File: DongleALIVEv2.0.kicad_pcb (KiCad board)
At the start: 2 copper layers, 45 x 55 mm, 76 parts, among them J1 C-OBD-II-16M, J2 Conn_01x05_Socket, J3 Conn_01x05_Socket, J4 USB_B_Micro, Q1 IRF5305S, Q2 SS8050-G, Q3 SS8050-G, SW1 SW_Push, SW2 SW_Push, SW3 SW_SPDT_321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

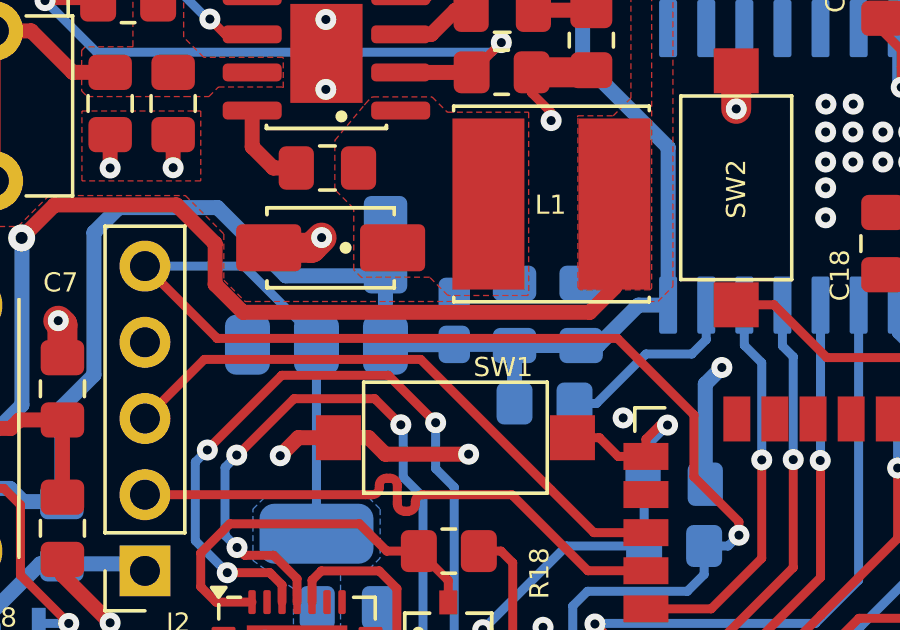
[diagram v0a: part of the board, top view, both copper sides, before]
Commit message: Fix tantalum capacitor & JLCPCB codes
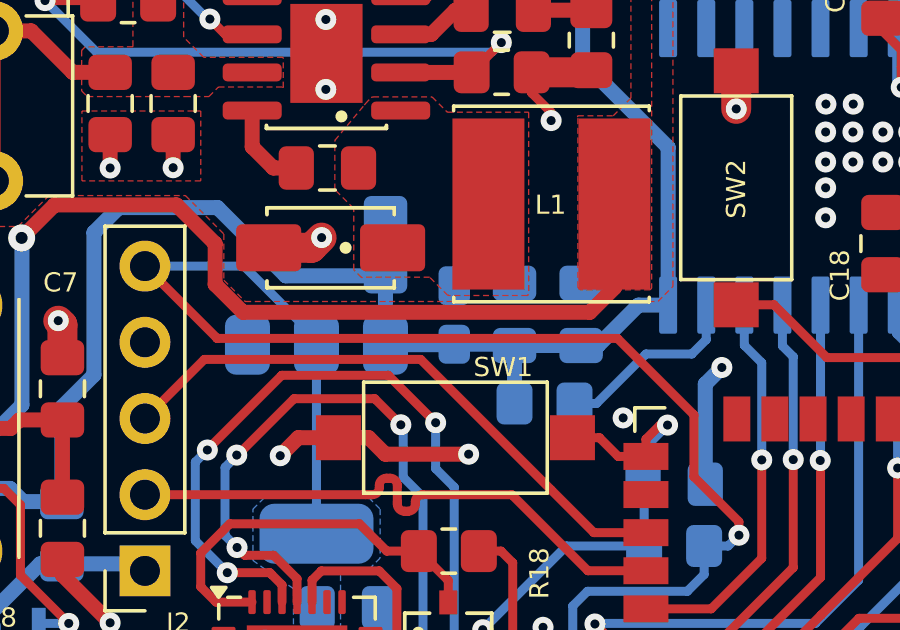
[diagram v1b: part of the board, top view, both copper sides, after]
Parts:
- C15, C17: value 0.1uF -> 100nF
- C16: footprint Capacitor_Tantalum_SMD:CP_EIA-1608-08_AVX-J_Pad1.25x1.05mm_HandSolder -> Capacitor_Tantalum_SMD:CP_EIA-2012-12_Kemet-R_Pad1.30x1.05mm_HandSolder
- moved C16 0.18 mm to (175.0, 95.8)

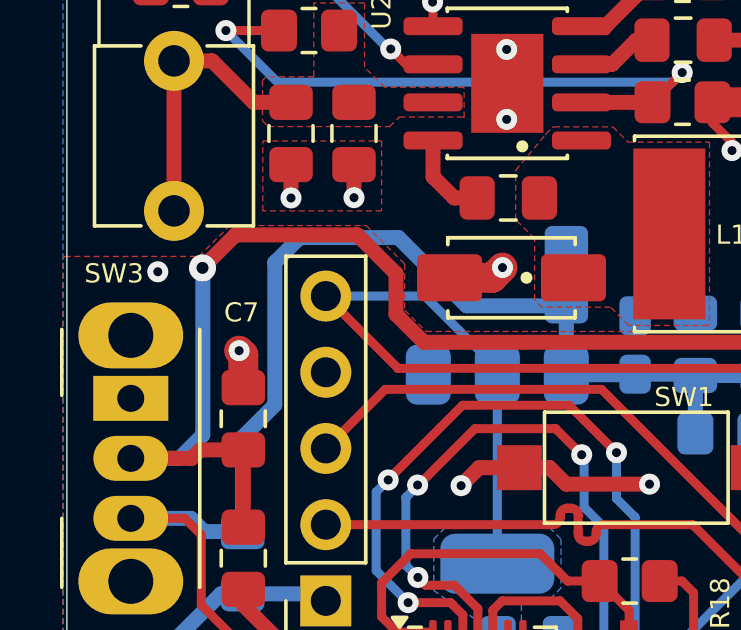
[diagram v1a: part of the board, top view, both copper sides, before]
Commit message: Testpoint to Vout
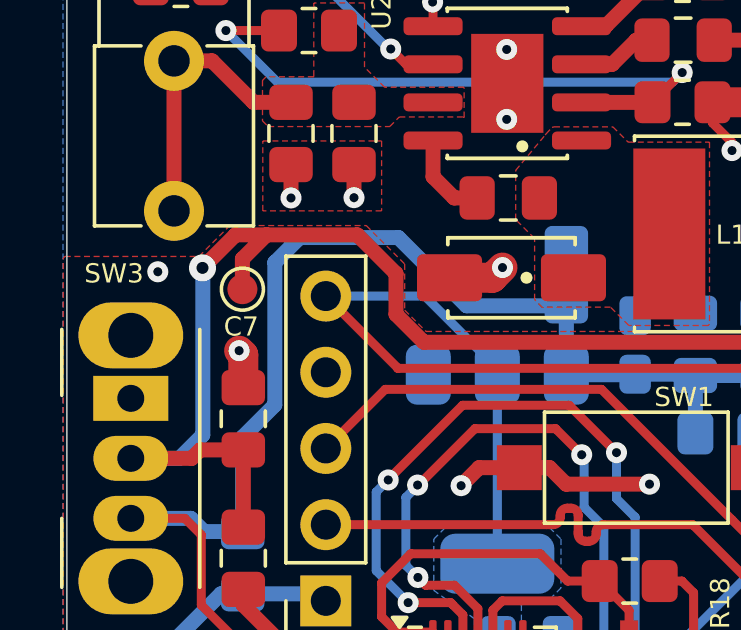
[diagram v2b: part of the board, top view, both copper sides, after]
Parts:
- added TP1: TestPoint, TestPoint:TestPoint_Pad_D1.0mm, F.Cu at (161.9, 93.9)
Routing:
- net /VoltageRegulatorESD/Vout: track 40.4 -> 42.5 mm
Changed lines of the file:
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@@
 		(allow_soldermask_bridges_in_footprints no)
 		(pcbplotparams
-			(layerselection 0x0000010_ffffffff)
+			(layerselection 0x00010fc_ffffffff)
 			(plot_on_all_layers_selection 0x0000000_00000000)
 			(disableapertmacros no)
@@
 			(sketchpadsonfab no)
 			(subtractmaskfromsilk no)
-			(outputformat 4)
+			(outputformat 1)
 			(mirror no)
-			(drillshape 2)
+			(drillshape 0)
 			(scaleselection 1)
-			(outputdirectory "01_Specs/02_LayoutPCB/")
+			(outputdirectory "02_Gerber&BOM/01_Gerber/00_Drill_Files/")
 		)
 	)
@@
 		(tags "capacitor handsolder")
 		(property "Reference" "C7"
-			(at 3.54 -0.06 180)
+			(at 3.07 -0.07 180)
 			(layer "F.SilkS")
 			(effects
@@
 			)
 		)
-		(property "LCSC" ""
+		(property "LCSC" "C157623"
 			(at 0 0 -90)
 			(unlocked yes)
@@
 		)
 	)
+	(footprint "TestPoint:TestPoint_Pad_D1.0mm"
+		(layer "F.Cu")
+		(at 161.93 93.91)
+		(descr "SMD pad as test Point, diameter 1.0mm")
+		(tags "test point SMD pad")
+		(property "Reference" "TP1"
+			(at 0 -1.448 0)
+			(layer "F.SilkS")
+			(hide yes)
+			(effects
+				(font
+					(size 1 1)
+					(thickness 0.15)
+				)
+			)
+		)
+		(property "Value" "TestPoint"
+			(at 0 1.55 0)
+			(layer "F.Fab")
+			(effects
+				(font
+					(size 1 1)
+					(thickness 0.15)
+				)
+			)
+		)
+		(property "Footprint" "TestPoint:TestPoint_Pad_D1.0mm"
+			(at 0 0 0)
+			(unlocked yes)
+			(layer "F.Fab")
+			(hide yes)
+			(effects
+				(font
+					(size 1.27 1.27)
+					(thickness 0.15)
+				)
+			)
+		)
+		(property "Datasheet" ""
+			(at 0 0 0)
+			(unlocked yes)
+			(layer "F.Fab")
+			(hide yes)
+			(effects
+				(font
+					(size 1.27 1.27)
+					(thickness 0.15)
+				)
+			)
+		)
+		(property "Description" "test point"
+			(at 0 0 0)
+			(unlocked yes)
+			(layer "F.Fab")
+			(hide yes)
+			(effects
+				(font
+					(size 1.27 1.27)
+					(thickness 0.15)
+				)
+			)
+		)
+		(property ki_fp_filters "Pin* Test*")
+		(sheetname "VoltageRegulatorESD")
+		(sheetfile "04_sch/VoltageRegulatorESD.kicad_sch")
+		(attr exclude_from_pos_files exclude_from_bom)
+		(fp_circle
+			(center 0 0)
+			(end 0 0.7)
+			(stroke
+				(width 0.12)
+				(type solid)
+			)
+			(fill none)
+			(layer "F.SilkS")
+		)
+		(fp_circle
+			(center 0 0)
+			(end 1 0)
+			(stroke
+				(width 0.05)
+				(type solid)
+			)
+			(fill none)
+			(layer "F.CrtYd")
+		)
+		(fp_text user "${REFERENCE}"
+			(at 0 -1.45 0)
+			(layer "F.Fab")
+			(effects
+				(font
+					(size 1 1)
+					(thickness 0.15)
+				)
+			)
+		)
+		(pad "1" smd circle
+			(at 0 0)
+			(size 1 1)
+			(layers "F.Cu" "F.Mask")
+			(net 19 "/VoltageRegulatorESD/Vout")
+			(pinfunction "1")
+			(pintype "passive")
+		)
+	)
 	(footprint "Capacitor_SMD:C_0805_2012Metric_Pad1.18x1.45mm_HandSolder"
 		(layer "F.Cu")
@@
 			)
 		)
-		(property "LCSC" ""
+		(property "LCSC" "C157623"
 			(at 0 0 -90)
 			(unlocked yes)
@@
 			)
 		)
-		(property "LCSC" ""
+		(property "LCSC" "C17513"
 			(at 0 0 -90)
 			(unlocked yes)
@@
 			)
 		)
-		(property "LCSC" ""
+		(property "LCSC" "C191101"
 			(at 0 0 180)
 			(unlocked yes)
@@
 			)
 		)
-		(property "LCSC" ""
+		(property "LCSC" "C82899"
 			(at 0 0 180)
 			(unlocked yes)
@@
 			)
 		)
-		(property "LCSC" ""
+		(property "LCSC" "C252310"
 			(at 0 0 -90)
 			(unlocked yes)
@@
 			)
 		)
-		(property "LCSC" ""
+		(property "LCSC" "C964632"
 			(at 0 0 0)
 			(unlocked yes)
@@
 			)
 		)
-		(property "LCSC" ""
+		(property "LCSC" "C191101"
 			(at 0 0 180)
 			(unlocked yes)
@@
 			)
 		)
-		(property "LCSC" ""
+		(property "LCSC" "C15850"
 			(at 0 0 -90)
 			(unlocked yes)
@@
 			)
 		)
-		(property "LCSC" ""
+		(property "LCSC" "C49678"
 			(at 0 0 90)
 			(unlocked yes)
@@
 			)
 		)
-		(property "LCSC" ""
+		(property "LCSC" "C124187"
 			(at 0 0 -90)
 			(unlocked yes)
@@
 			)
 		)
-		(property "LCSC" ""
+		(property "LCSC" "C5250735"
 			(at 0 0 -90)
 			(unlocked yes)
@@
 			)
 		)
-		(property "LCSC" ""
+		(property "LCSC" "C201218"
 			(at 0 0 -90)
 			(unlocked yes)
@@
 			)
 		)
-		(property "LCSC" ""
+		(property "LCSC" "C15850"
 			(at 0 0 -90)
 			(unlocked yes)
@@
 			)
 		)
-		(property "LCSC" ""
+		(property "LCSC" "C917183"
 			(at 0 0 -90)
 			(unlocked yes)
@@
 			)
 		)
-		(property "LCSC" ""
+		(property "LCSC" "C966144"
 			(at 0 0 -90)
 			(unlocked yes)
@@
 			)
 		)
-		(property "LCSC" ""
+		(property "LCSC" "C15850"
 			(at 0 0 90)
 			(unlocked yes)
@@
 	)
 	(segment
-		(start 161.96 96.1)
-		(end 161.82 95.96)
-		(width 1)
-		(layer "F.Cu")
-		(net 12)
-	)
-	(segment
 		(start 163.55 90.87)
 		(end 163.55 89.7575)
@@
 	)
 	(segment
-		(start 161.96 97.1925)
-		(end 161.96 96.1)
-		(width 1)
-		(layer "F.Cu")
-		(net 12)
-	)
-	(segment
 		(start 170.26 93.53)
 		(end 170.6 93.19)
@@
 	)
 	(segment
+		(start 161.82 95.96)
+		(end 161.96 96.1)
+		(width 1)
+		(layer "F.Cu")
+		(net 12)
+	)
+	(segment
 		(start 163.55 106.03)
 		(end 161.96 104.44)
@@
 	)
 	(segment
+		(start 161.96 96.1)
+		(end 161.96 97.1925)
+		(width 1)
+		(layer "F.Cu")
+		(net 12)
+	)
+	(segment
 		(start 188.69 117.59)
 		(end 186.15 117.59)
@@
 	)
 	(segment
+		(start 162.73 92.1)
+		(end 165.76 92.1)
+		(width 0.5)
+		(layer "F.Cu")
+		(net 19)
+	)
+	(segment
+		(start 161.7 92.1)
+		(end 162.73 92.1)
+		(width 0.5)
+		(layer "F.Cu")
+		(net 19)
+	)
+	(segment
 		(start 158.21 99.55)
 		(end 160.24 99.55)
@@
 	)
 	(segment
+		(start 161.93 92.9)
+		(end 161.93 93.91)
+		(width 0.5)
+		(layer "F.Cu")
+		(net 19)
+	)
+	(segment
 		(start 167.98 95.68)
 		(end 179.54 95.68)
@@
 	)
 	(segment
-		(start 161.7 92.1)
-		(end 165.76 92.1)
+		(start 162.73 92.1)
+		(end 161.93 92.9)
 		(width 0.5)
 		(layer "F.Cu")

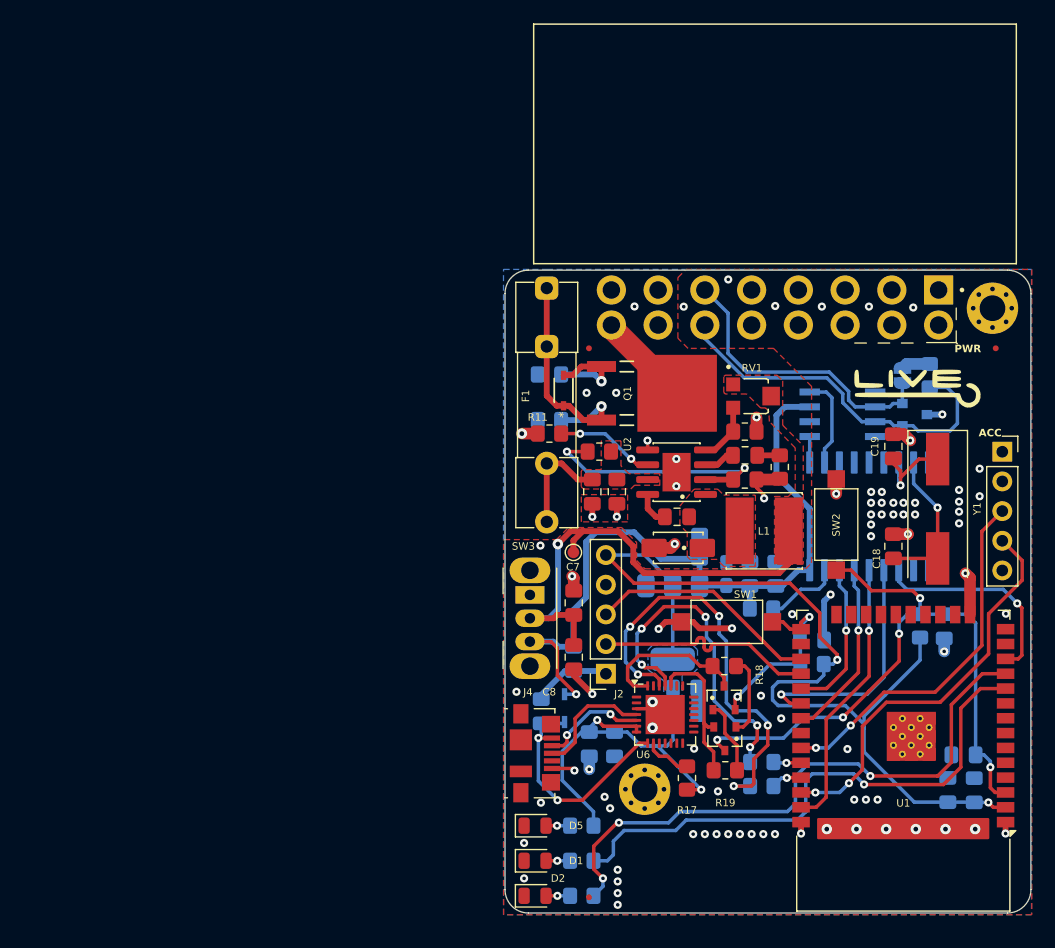
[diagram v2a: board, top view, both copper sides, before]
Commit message: Add step file of the PCB
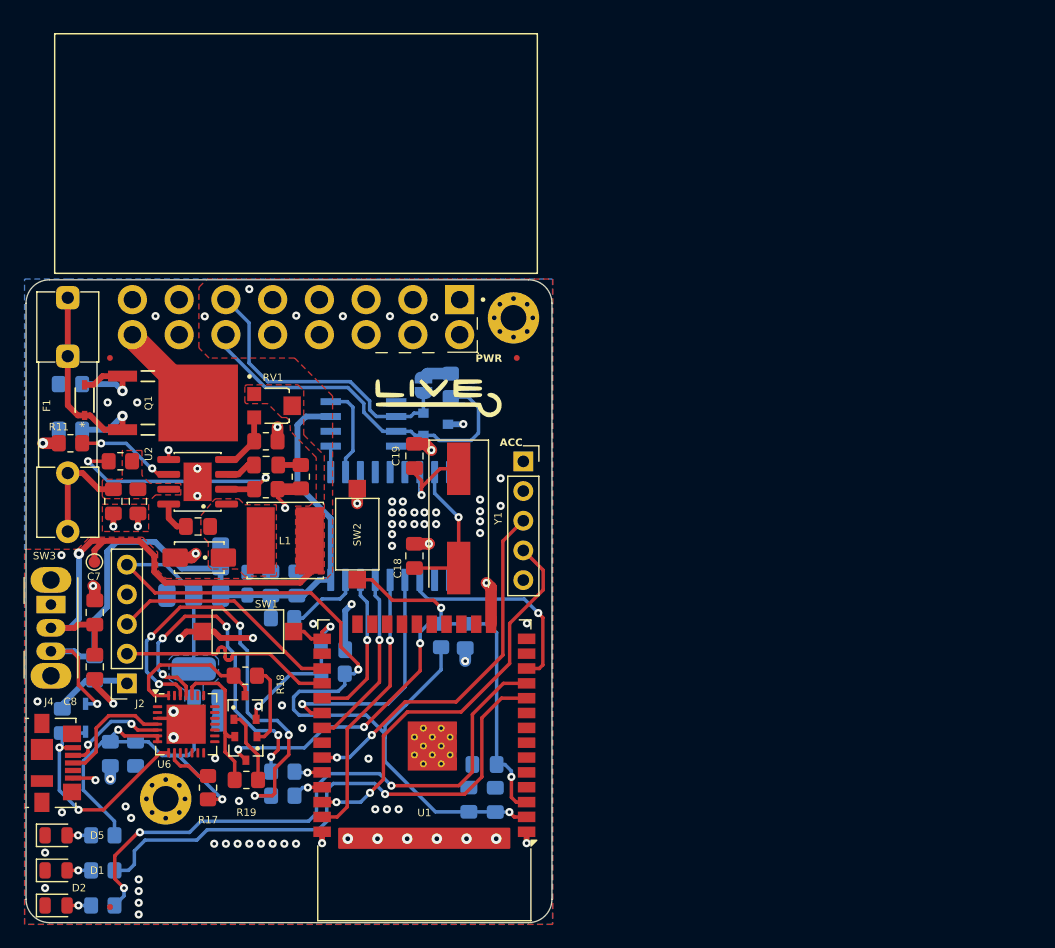
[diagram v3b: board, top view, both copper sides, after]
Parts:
- moved C11 41.0 mm to (135.6, 86.4)
- moved C13 41.0 mm to (130.5, 108.5)
- moved C14 41.0 mm to (130.5, 106.4)
- moved C15 41.0 mm to (136.0, 96.6)
- moved C16 41.0 mm to (134.0, 96.6)
- moved C17 41.0 mm to (138.3, 96.6)
- moved C18 41.0 mm to (148.3, 94.2)
- moved C19 41.0 mm to (148.3, 85.7)
- moved C23 41.0 mm to (118.2, 108.3)
- moved C4 41.0 mm to (154.3, 112.1)
- moved C7 41.0 mm to (121.0, 99.1)
- moved C8 41.0 mm to (121.0, 103.7)
- moved C9 41.0 mm to (122.6, 89.5)
- moved D3 41.0 mm to (129.9, 94.4)
- moved D6 41.0 mm to (150.1, 83.0)
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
